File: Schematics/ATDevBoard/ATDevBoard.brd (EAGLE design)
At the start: 68.5 x 55.1 mm, 39 parts, among them U1 TINY85-DIP

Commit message: Rerun cam on brd file to upload to SeeedStudio, deleted PNG folder
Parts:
- removed C9: 100n, rcl:C050-024X044
- added C5: 100n, SmartPrj:C050-024X044
- C6: value 100n -> 22p
- C7: value 22p -> 100n; device SmartPrj:C050-024X044 -> rcl:C050-024X044
- moved C7 33.8 mm to (16.0, 45.7)
- moved C6 29.7 mm to (49.3, 51.6)
- moved C8 17.8 mm to (15.5, 27.9)
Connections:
- net GND: now also C5.1, C6.2, C7.1; no longer C6.1, C7.2, C9.1
- net VCC: now also C5.2, C8.2; no longer C6.2, C9.2
- net VIN: now also C7.2; no longer C8.2
- net XTAL1: now also C6.1; no longer C7.1
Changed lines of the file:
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@@
 </element>
 <element name="C2" library="SmartPrj" package="C050-024X044" value="100n" x="39.116" y="27.94"/>
-<element name="C8" library="rcl" package="C050-024X044" value="100n" x="16.002" y="45.72" smashed="yes">
+<element name="C7" library="rcl" package="C050-024X044" value="100n" x="16.002" y="45.72" smashed="yes">
 <attribute name="NAME" x="13.843" y="47.117" size="1.27" layer="25" ratio="10"/>
 <attribute name="VALUE" x="13.843" y="43.053" size="1.27" layer="27" ratio="10"/>
 </element>
-<element name="C9" library="rcl" package="C050-024X044" value="100n" x="15.494" y="27.94"/>
+<element name="C8" library="rcl" package="C050-024X044" value="100n" x="15.494" y="27.94"/>
 <element name="C4" library="SmartPrj" package="C050-024X044" value="100n" x="23.368" y="27.94"/>
-<element name="C6" library="SmartPrj" package="C050-024X044" value="100n" x="31.242" y="27.94"/>
+<element name="C5" library="SmartPrj" package="C050-024X044" value="100n" x="31.242" y="27.94"/>
 <element name="D1" library="diode" package="DO41-10" value="1N4007" x="34.544" y="48.26" smashed="yes" rot="R180">
 <attribute name="NAME" x="39.116" y="50.165" size="1.27" layer="25" ratio="10" rot="R180"/>
@@
 <attribute name="NAME" x="65.8622" y="54.8132" size="1.27" layer="25" ratio="10" rot="R180"/>
 </element>
-<element name="R7" library="rcl" package="0207/10" value="1M" x="42.926" y="48.006" rot="R270"/>
+<element name="R7" library="rcl" package="0207/10" value="1M" x="42.926" y="48.006" smashed="yes" rot="R270">
+<attribute name="NAME" x="42.418" y="49.276" size="1.27" layer="25" ratio="10" rot="R270"/>
+<attribute name="VALUE" x="42.291" y="50.2666" size="1.27" layer="27" ratio="10" rot="R270"/>
+</element>
 <element name="R1" library="rcl" package="0204/7" value="220" x="21.59" y="37.084" smashed="yes" rot="R270">
 <attribute name="NAME" x="21.1074" y="36.576" size="0.9906" layer="25" ratio="10" rot="R270"/>
@@
 <attribute name="VALUE" x="54.991" y="48.895" size="1.27" layer="27" ratio="10"/>
 </element>
-<element name="C7" library="SmartPrj" package="C050-024X044" value="22p" x="49.276" y="51.562" smashed="yes">
+<element name="C6" library="SmartPrj" package="C050-024X044" value="22p" x="49.276" y="51.562" smashed="yes">
 <attribute name="NAME" x="47.117" y="52.959" size="1.27" layer="25" ratio="10"/>
 <attribute name="VALUE" x="47.117" y="48.895" size="1.27" layer="27" ratio="10"/>
@@
 <contactref element="IOH" pad="7"/>
 <contactref element="C4" pad="1"/>
-<contactref element="C9" pad="1"/>
 <contactref element="C8" pad="1"/>
+<contactref element="C7" pad="1"/>
 <contactref element="ICSP_10" pad="8"/>
 <contactref element="ICSP_10" pad="10"/>
@@
 <contactref element="MCU1" pad="14"/>
 <contactref element="SCK" pad="C"/>
-<contactref element="C6" pad="1"/>
+<contactref element="C5" pad="1"/>
 <contactref element="ZU4" pad="8"/>
 <contactref element="ZU4" pad="22"/>
 <contactref element="SW1" pad="P$2"/>
 <contactref element="C3" pad="1"/>
-<contactref element="C7" pad="2"/>
+<contactref element="C6" pad="2"/>
 <contactref element="ON" pad="C"/>
 <contactref element="JPOWER" pad="1"/>
@@
 </signal>
 <signal name="VIN" class="1">
-<contactref element="C8" pad="2"/>
+<contactref element="C7" pad="2"/>
 <contactref element="D3" pad="C"/>
 <contactref element="POWER" pad="5"/>
@@
 <contactref element="R7" pad="1"/>
 <contactref element="OSC1" pad="1"/>
-<contactref element="C7" pad="1"/>
+<contactref element="C6" pad="1"/>
 <wire x1="50.292" y1="48.006" x2="50.292" y2="45.72" width="0.254" layer="1"/>
 <wire x1="46.736" y1="51.562" x2="50.292" y2="48.006" width="0.254" layer="1"/>
@@
 <contactref element="ZU4" pad="7"/>
 <contactref element="ZU4" pad="20"/>
-<contactref element="C6" pad="2"/>
-<contactref element="C9" pad="2"/>
+<contactref element="C5" pad="2"/>
+<contactref element="C8" pad="2"/>
 <contactref element="POWER" pad="4"/>
 <contactref element="U1" pad="8"/>

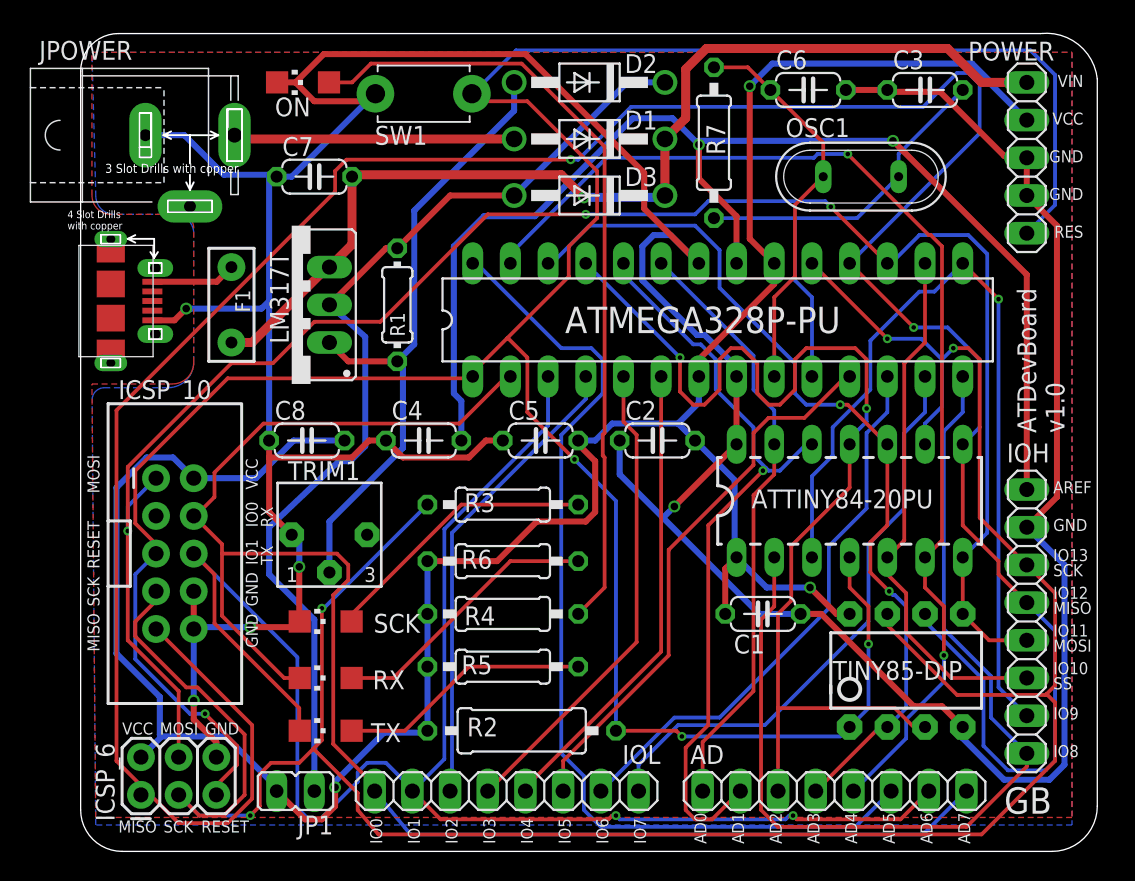
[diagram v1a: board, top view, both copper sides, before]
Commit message: Fixed 1M resistor package, and header distance in PCB
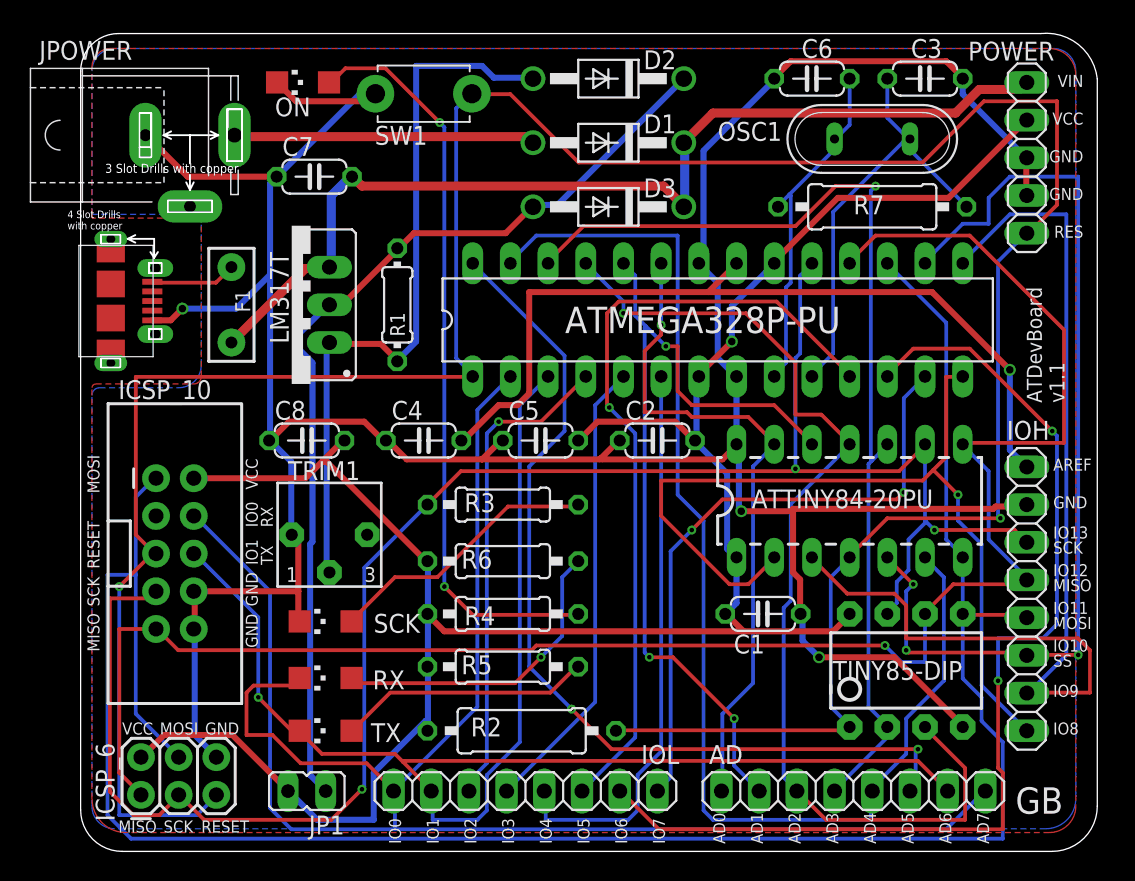
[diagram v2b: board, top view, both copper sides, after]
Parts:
- R7: device rcl:0207/10 -> rcl:0309/12
- moved R7 11.5 mm to (53.6, 43.7), turned to 0 degrees
- moved OSC1 2.65 mm to (53.6, 48.3)
- moved IOH 1.52 mm to (64.0, 17.3)
- moved D3 1.48 mm to (35.8, 43.7)
- moved D1 1.30 mm to (35.8, 48.0)
- moved D2 1.30 mm to (35.8, 52.3)
- moved IOL 1.27 mm to (30.2, 4.32)
- moved AD 1.27 mm to (52.3, 4.32)
- moved C6 0.80 mm to (49.5, 52.3), turned to 180 degrees
- moved C3 0.76 mm to (57.1, 52.3), turned to 180 degrees
- moved JP1 0.76 mm to (15.5, 4.32)
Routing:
- net MISO: track 191.9 -> 121.8 mm, vias 2 -> 1
- net SCK: track 175.0 -> 126.7 mm, vias 4 -> 3
- net GND: track 265.2 -> 221.4 mm, vias 5 -> 3
- net IO6: track 37.7 -> 71.6 mm, vias 0 -> 2
- net SS: track 35.9 -> 65.0 mm, vias 0 -> 3
- net AREF: track 83.7 -> 57.0 mm, vias 2 -> 1
- net MOSI: track 123.7 -> 146.1 mm, vias 3 -> 0
- net VCC: track 169.3 -> 148.1 mm, vias 3 -> 1
- net IO5: track 37.5 -> 53.4 mm, vias 0 -> 1
- net IO0: track 108.8 -> 123.9 mm
- net IO9: track 56.9 -> 71.6 mm, vias 1 -> 0
- net IO1: track 114.4 -> 100.3 mm, vias 2 -> 1
- net AD3: track 60.4 -> 68.8 mm, vias 2 -> 1
- net AD4: track 75.3 -> 83.4 mm, vias 2 -> 0
- net IO8: track 66.6 -> 59.3 mm, vias 0 -> 1
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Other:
- board text added: "ATDevBoard v1.1"
- board text removed: "ATDevBoard v1.0"
